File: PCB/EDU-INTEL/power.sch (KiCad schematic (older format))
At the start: 13 parts, among them P4 5V_IN, P5 5V_IN, U11 NCP1117ST33T3G, U12 NCP1117ST18T3G

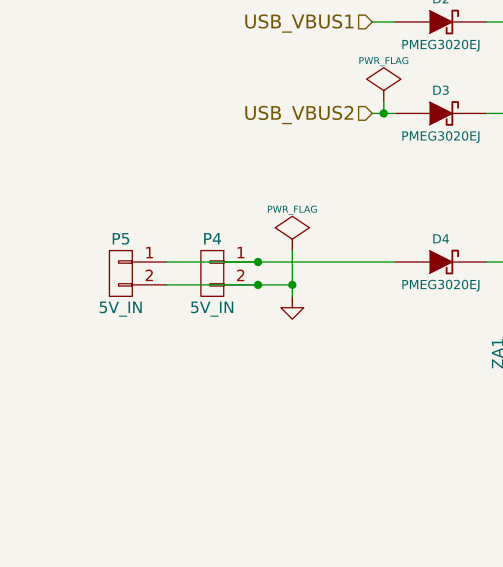
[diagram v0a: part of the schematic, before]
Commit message: EDU-CIAA-INTEL: replaced terminal block for DC barrel jack connector
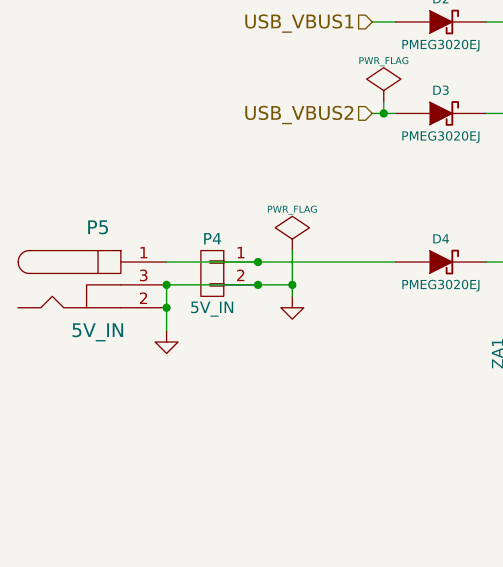
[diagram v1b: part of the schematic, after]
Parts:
- removed P5: 5V_IN, Pin_Headers:Pin_Header_Straight_1x02, symbol CONN_01X02
- added P5: 5V_IN, Connect:BARREL_JACK, symbol BARREL_JACK
- P4: footprint Connect:bornier2 -> Pin_Headers:Pin_Header_Straight_1x02
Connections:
- net GND: now also P5.2, P5.3
- net at D4.1 (A), P4.1 (P1): now also P5.1
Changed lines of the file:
@@
 F 0 "P4" H 4800 3450 50  0000 C CNN
 F 1 "5V_IN" H 4800 3150 50  0000 C CNN
-F 2 "Connect:bornier2" H 4800 3300 60  0001 C CNN
+F 2 "Pin_Headers:Pin_Header_Straight_1x02" H 4800 3300 60  0001 C CNN
 F 3 "" H 4800 3300 60  0000 C CNN
 	1    4800 3300
 	-1   0    0    -1
 $EndComp
-$Comp
-L CONN_01X02 P5
-U 1 1 54DE8D79
-P 4400 3300
-F 0 "P5" H 4400 3450 50  0000 C CNN
-F 1 "5V_IN" H 4400 3150 50  0000 C CNN
-F 2 "Pin_Headers:Pin_Header_Straight_1x02" H 4400 3300 60  0001 C CNN
-F 3 "" H 4400 3300 60  0000 C CNN
-	1    4400 3300
-	-1   0    0    -1
-$EndComp
 Connection ~ 5000 3250
 Connection ~ 5000 3350
+$Comp
+L BARREL_JACK P5
+U 1 1 553529D0
+P 4300 3350
+F 0 "P5" H 4300 3600 60  0000 C CNN
+F 1 "5V_IN" H 4300 3150 60  0000 C CNN
+F 2 "Connect:BARREL_JACK" H 4300 3350 60  0001 C CNN
+F 3 "" H 4300 3350 60  0000 C CNN
+	1    4300 3350
+	1    0    0    -1
+$EndComp
+Wire Wire Line
+	4600 3350 4600 3550
+Connection ~ 4600 3450
+$Comp
+L GND #PWR098
+U 1 1 55352B92
+P 4600 3550
+F 0 "#PWR098" H 4600 3550 30  0001 C CNN
+F 1 "GND" H 4600 3480 30  0001 C CNN
+F 2 "" H 4600 3550 60  0000 C CNN
+F 3 "" H 4600 3550 60  0000 C CNN
+	1    4600 3550
+	1    0    0    -1
+$EndComp
+Connection ~ 4600 3350
 $EndSCHEMATC
